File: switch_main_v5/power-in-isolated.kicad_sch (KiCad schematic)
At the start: 13 parts, among them J601 MKXS1-1 Power Input, U601 TVS3301DRBR, U602 TPS26600RHFR

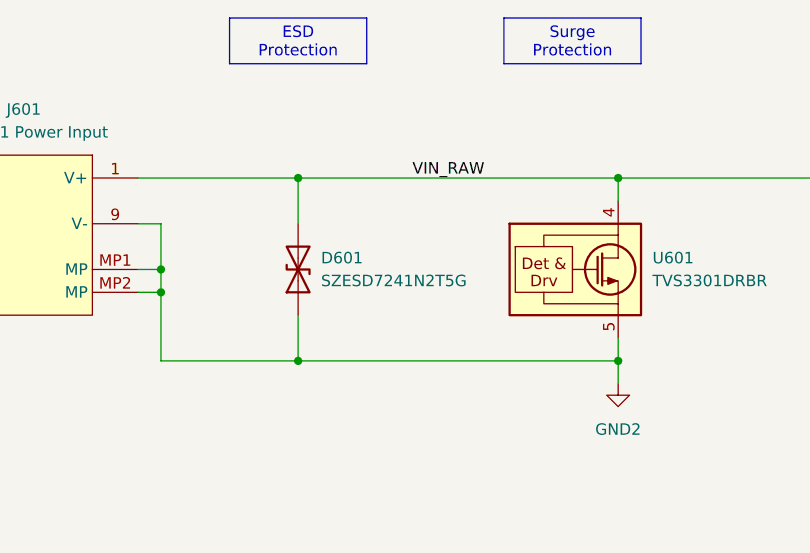
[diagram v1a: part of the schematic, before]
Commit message: Changed main 3V3 regulator to 3A, added switch 2 crystal & other changes
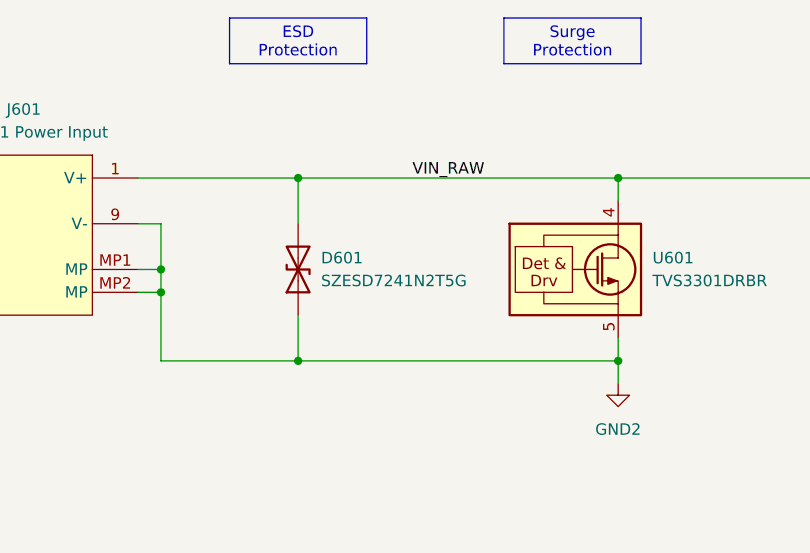
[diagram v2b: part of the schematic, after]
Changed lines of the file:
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@@
 	(symbol
 		(lib_id "TVS:SZESD7241N2T5G")
-		(at 55.88 81.28 90)
+		(at 58.42 81.28 90)
 		(unit 1)
 		(exclude_from_sim no)
@@
 		(on_board yes)
 		(dnp no)
-		(fields_autoplaced yes)
 		(property "Reference" "D601"
-			(at 60.96 80.0099 90)
+			(at 60.96 80.01 90)
 			(effects
 				(font
@@
 		)
 		(property "Value" "SZESD7241N2T5G"
-			(at 60.96 82.5499 90)
+			(at 60.96 82.55 90)
 			(effects
 				(font
@@
 		)
 		(property "Footprint" "project_footprints:SZESD7462N2T5G"
-			(at 66.04 97.79 0)
+			(at 68.58 97.79 0)
 			(effects
 				(font
@@
 		)
 		(property "Datasheet" "https://www.onsemi.com/pub/Collateral/ESD7241-D.PDF"
-			(at 68.58 110.49 0)
+			(at 71.12 110.49 0)
 			(effects
 				(font
@@
 		)
 		(property "Description" "SZESD7241MXWT5G Wettable Flank Package; SZ Prefix for Automotive and Other Applications Requiring Unique Site and Control Change Requirements; AECQ101 Qualified and PPAP CapableSZ Prefix for Automotive and Other Applications Requiring Unique Site and Control Change Requirements; AECQ101 Qualified and PPAP Capable; Ultra-Low Capacitance: < 1.0pF Max; Low Leakage: < 0.5uA; IEC61000-4-2 (ESD): Level 4 +/-28kV Contact; IEC61000-4-4 (EFT): 40A - 5/50ns; IEC61000-4-5 (Lightning): 1A - 8/20us; These Devices are Pb"
-			(at 62.23 81.28 0)
+			(at 64.77 81.28 0)
 			(effects
 				(font
@@
 		)
 		(property "Height" "0.4"
-			(at 71.12 82.55 0)
+			(at 73.66 82.55 0)
 			(effects
 				(font
@@
 		)
 		(property "Mouser Part Number" "863-SZESD7241N2T5G"
-			(at 73.66 92.71 0)
+			(at 76.2 92.71 0)
 			(effects
 				(font
@@
 		)
 		(property "Mouser Price/Stock" "https://www.mouser.co.uk/ProductDetail/onsemi/SZESD7241N2T5G?qs=z6PAvqrnkvSq0oMCl81g4Q%3D%3D"
-			(at 76.2 130.81 0)
+			(at 78.74 130.81 0)
 			(effects
 				(font
@@
 		)
 		(property "Manufacturer_Name" "onsemi"
-			(at 78.74 85.09 0)
+			(at 81.28 85.09 0)
 			(effects
 				(font
@@
 		)
 		(property "Manufacturer_Part_Number" "SZESD7241N2T5G"
-			(at 81.28 90.17 0)
+			(at 83.82 90.17 0)
 			(effects
 				(font

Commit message: Placed 1000BASE-T PHY decoupling capacitors
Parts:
- J601: footprint project_footprints:10132798-031100LF -> project_footprints:10132797-031100LF
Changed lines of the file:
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@@
 			)
 		)
-		(property "Footprint" "project_footprints:10132798-031100LF"
+		(property "Footprint" "project_footprints:10132797-031100LF"
 			(at 27.94 88.9 0)
 			(effects

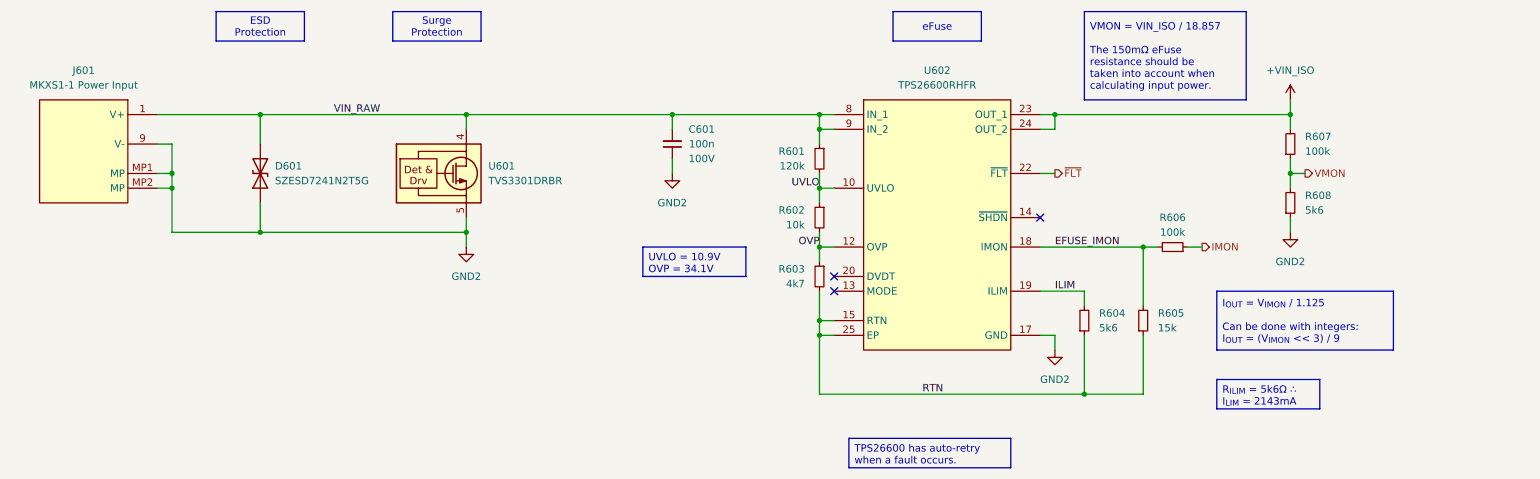
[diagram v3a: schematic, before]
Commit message: Changed primary side input current limit to 545mA (from 255mA which is less than the max possible load current of 326mA)
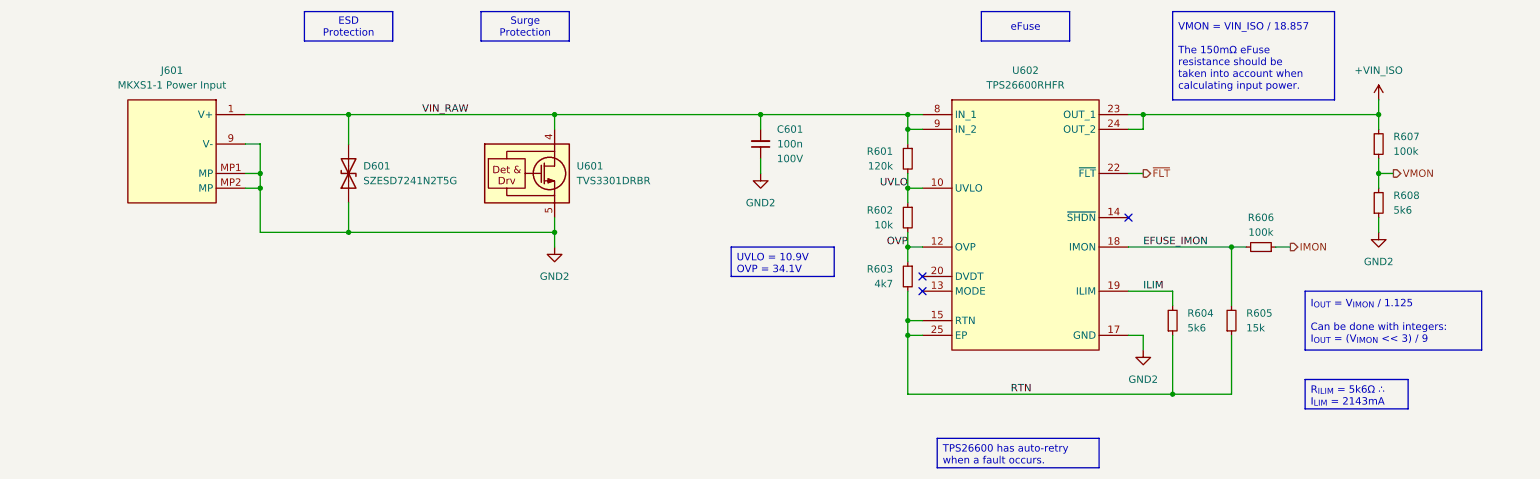
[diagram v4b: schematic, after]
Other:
- moved on the sheet: C601, D601, J601, R601, R602, R603, R604, R605, R606, R607, R608, U601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

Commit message: Tidied schematic and PCB
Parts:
- renumbered C601 to C1201, D601 to D1201, J601 to J1201, R607 to R1201, R601 to R1202, R608 to R1203, R602 to R1204, R606 to R1205, R603 to R1206, R604 to R1207, R605 to R1208, U602 to U1201, U601 to U1202
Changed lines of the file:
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@@
 		(dnp no)
 		(fields_autoplaced yes)
-		(property "Reference" "U602"
+		(property "Reference" "U1201"
 			(at 190.5 63.5 0)
 			(effects
@@
 			(project "switch_main_v4"
 				(path "/a5e57332-4284-4d3c-ab3c-13bc0ddb29b6/b1ff42f5-7cae-489e-9f8e-588cc93f3151/b2e985e0-3ca0-4c8f-ac20-521f3b79109e"
-					(reference "U602")
+					(reference "U1201")
 					(unit 1)
 				)
@@
 		(dnp no)
 		(fields_autoplaced yes)
-		(property "Reference" "#PWR0604"
+		(property "Reference" "#PWR01201"
 			(at 251.46 72.39 0)
 			(effects
@@
 			(project "switch_main_v4"
 				(path "/a5e57332-4284-4d3c-ab3c-13bc0ddb29b6/b1ff42f5-7cae-489e-9f8e-588cc93f3151/b2e985e0-3ca0-4c8f-ac20-521f3b79109e"
-					(reference "#PWR0604")
+					(reference "#PWR01201")
 					(unit 1)
 				)
@@
 		(on_board yes)
 		(dnp no)
-		(property "Reference" "D601"
+		(property "Reference" "D1201"
 			(at 76.2 80.01 90)
 			(effects
@@
 			(project "switch_main_v4"
 				(path "/a5e57332-4284-4d3c-ab3c-13bc0ddb29b6/b1ff42f5-7cae-489e-9f8e-588cc93f3151/b2e985e0-3ca0-4c8f-ac20-521f3b79109e"
-					(reference "D601")
+					(reference "D1201")
 					(unit 1)
 				)
@@
 		(dnp no)
 		(fields_autoplaced yes)
-		(property "Reference" "#PWR0605"
+		(property "Reference" "#PWR01203"
 			(at 251.46 97.79 0)
 			(effects
@@
 			(project "switch_main_v4"
 				(path "/a5e57332-4284-4d3c-ab3c-13bc0ddb29b6/b1ff42f5-7cae-489e-9f8e-588cc93f3151/b2e985e0-3ca0-4c8f-ac20-521f3b79109e"
-					(reference "#PWR0605")
+					(reference "#PWR01203")
 					(unit 1)
 				)
@@
 		(dnp no)
 		(fields_autoplaced yes)
-		(property "Reference" "#PWR0603"
+		(property "Reference" "#PWR01205"
 			(at 210.82 118.11 0)
 			(effects
@@
 			(project "switch_main_v4"
 				(path "/a5e57332-4284-4d3c-ab3c-13bc0ddb29b6/b1ff42f5-7cae-489e-9f8e-588cc93f3151/b2e985e0-3ca0-4c8f-ac20-521f3b79109e"
-					(reference "#PWR0603")
+					(reference "#PWR01205")
 					(unit 1)
 				)
@@
 		(dnp no)
 		(fields_autoplaced yes)
-		(property "Reference" "#PWR0601"
+		(property "Reference" "#PWR01204"
 			(at 109.22 100.33 0)
 			(effects
@@
 			(project "switch_main_v4"
 				(path "/a5e57332-4284-4d3c-ab3c-13bc0ddb29b6/b1ff42f5-7cae-489e-9f8e-588cc93f3151/b2e985e0-3ca0-4c8f-ac20-521f3b79109e"
-					(reference "#PWR0601")
+					(reference "#PWR01204")
 					(unit 1)
 				)
@@
 		(on_board yes)
 		(dnp no)
-		(property "Reference" "R601"
+		(property "Reference" "R1202"
 			(at 167.64 77.4699 0)
 			(effects
@@
 			(project "switch_main_v4"
 				(path "/a5e57332-4284-4d3c-ab3c-13bc0ddb29b6/b1ff42f5-7cae-489e-9f8e-588cc93f3151/b2e985e0-3ca0-4c8f-ac20-521f3b79109e"
-					(reference "R601")
+					(reference "R1202")
 					(unit 1)
 				)
@@
 		(on_board yes)
 		(dnp no)
-		(property "Reference" "C601"
+		(property "Reference" "C1201"
 			(at 149.86 73.66 0)
 			(effects
@@
 			(project "switch_main_v4"
 				(path "/a5e57332-4284-4d3c-ab3c-13bc0ddb29b6/b1ff42f5-7cae-489e-9f8e-588cc93f3151/b2e985e0-3ca0-4c8f-ac20-521f3b79109e"
-					(reference "C601")
+					(reference "C1201")
 					(unit 1)
 				)
@@
 		(dnp no)
 		(fields_autoplaced yes)
-		(property "Reference" "J601"
+		(property "Reference" "J1201"
 			(at 43.18 63.5 0)
 			(effects
@@
 			(project "switch_main_v4"
 				(path "/a5e57332-4284-4d3c-ab3c-13bc0ddb29b6/b1ff42f5-7cae-489e-9f8e-588cc93f3151/b2e985e0-3ca0-4c8f-ac20-521f3b79109e"
-					(reference "J601")
+					(reference "J1201")
 					(unit 1)
 				)
@@
 		(on_board yes)
 		(dnp no)
-		(property "Reference" "R602"
+		(property "Reference" "R1204"
 			(at 167.64 87.6299 0)
 			(effects
@@
 			(project "switch_main_v4"
 				(path "/a5e57332-4284-4d3c-ab3c-13bc0ddb29b6/b1ff42f5-7cae-489e-9f8e-588cc93f3151/b2e985e0-3ca0-4c8f-ac20-521f3b79109e"
-					(reference "R602")
+					(reference "R1204")
 					(unit 1)
 				)
@@
 		(on_board yes)
 		(dnp no)
-		(property "Reference" "R605"
+		(property "Reference" "R1208"
 			(at 228.6 105.4101 0)
 			(effects
@@
 			(project "switch_main_v4"
 				(path "/a5e57332-4284-4d3c-ab3c-13bc0ddb29b6/b1ff42f5-7cae-489e-9f8e-588cc93f3151/b2e985e0-3ca0-4c8f-ac20-521f3b79109e"
-					(reference "R605")
+					(reference "R1208")
 					(unit 1)
 				)
@@
 		(dnp no)
 		(fields_autoplaced yes)
-		(property "Reference" "U601"
+		(property "Reference" "U1202"
 			(at 113.03 80.0099 0)
 			(effects
@@
 			(project "switch_main_v4"
 				(path "/a5e57332-4284-4d3c-ab3c-13bc0ddb29b6/b1ff42f5-7cae-489e-9f8e-588cc93f3151/b2e985e0-3ca0-4c8f-ac20-521f3b79109e"
-					(reference "U601")
+					(reference "U1202")
 					(unit 1)
 				)
@@
 		(on_board yes)
 		(dnp no)
-		(property "Reference" "R608"
+		(property "Reference" "R1203"
 			(at 254 85.09 0)
 			(effects
@@
 			(project "switch_main_v4"
 				(path "/a5e57332-4284-4d3c-ab3c-13bc0ddb29b6/b1ff42f5-7cae-489e-9f8e-588cc93f3151/b2e985e0-3ca0-4c8f-ac20-521f3b79109e"
-					(reference "R608")
+					(reference "R1203")
 					(unit 1)
 				)
@@
 		(on_board yes)
 		(dnp no)
-		(property "Reference" "R603"
+		(property "Reference" "R1206"
 			(at 167.64 97.7899 0)
 			(effects
@@
 			(project "switch_main_v4"
 				(path "/a5e57332-4284-4d3c-ab3c-13bc0ddb29b6/b1ff42f5-7cae-489e-9f8e-588cc93f3151/b2e985e0-3ca0-4c8f-ac20-521f3b79109e"
-					(reference "R603")
+					(reference "R1206")
 					(unit 1)
 				)
@@
 		(on_board yes)
 		(dnp no)
-		(property "Reference" "R604"
+		(property "Reference" "R1207"
 			(at 218.44 105.4101 0)
 			(effects
@@
 			(project "switch_main_v4"
 				(path "/a5e57332-4284-4d3c-ab3c-13bc0ddb29b6/b1ff42f5-7cae-489e-9f8e-588cc93f3151/b2e985e0-3ca0-4c8f-ac20-521f3b79109e"
-					(reference "R604")
+					(reference "R1207")
 					(unit 1)
 				)
@@
 		(on_board yes)
 		(dnp no)
-		(property "Reference" "R607"
+		(property "Reference" "R1201"
 			(at 254 74.93 0)
 			(effects
@@
 			(project "switch_main_v4"
 				(path "/a5e57332-4284-4d3c-ab3c-13bc0ddb29b6/b1ff42f5-7cae-489e-9f8e-588cc93f3151/b2e985e0-3ca0-4c8f-ac20-521f3b79109e"
-					(reference "R607")
+					(reference "R1201")
 					(unit 1)
 				)
@@
 		(on_board yes)
 		(dnp no)
-		(property "Reference" "R606"
+		(property "Reference" "R1205"
 			(at 231.14 88.9 90)
 			(effects
@@
 			(project "switch_main_v4"
 				(path "/a5e57332-4284-4d3c-ab3c-13bc0ddb29b6/b1ff42f5-7cae-489e-9f8e-588cc93f3151/b2e985e0-3ca0-4c8f-ac20-521f3b79109e"
-					(reference "R606")
+					(reference "R1205")
 					(unit 1)
 				)
@@
 		(dnp no)
 		(fields_autoplaced yes)
-		(property "Reference" "#PWR0602"
+		(property "Reference" "#PWR01202"
 			(at 144.78 87.63 0)
 			(effects
@@
 			(project "switch_main_v4"
 				(path "/a5e57332-4284-4d3c-ab3c-13bc0ddb29b6/b1ff42f5-7cae-489e-9f8e-588cc93f3151/b2e985e0-3ca0-4c8f-ac20-521f3b79109e"
-					(reference "#PWR0602")
-					(unit 1)
-				)
+					(reference "#PWR01202")
+					(unit 1)
+				)
